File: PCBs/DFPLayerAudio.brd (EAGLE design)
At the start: 45.4 x 33 mm, 13 parts

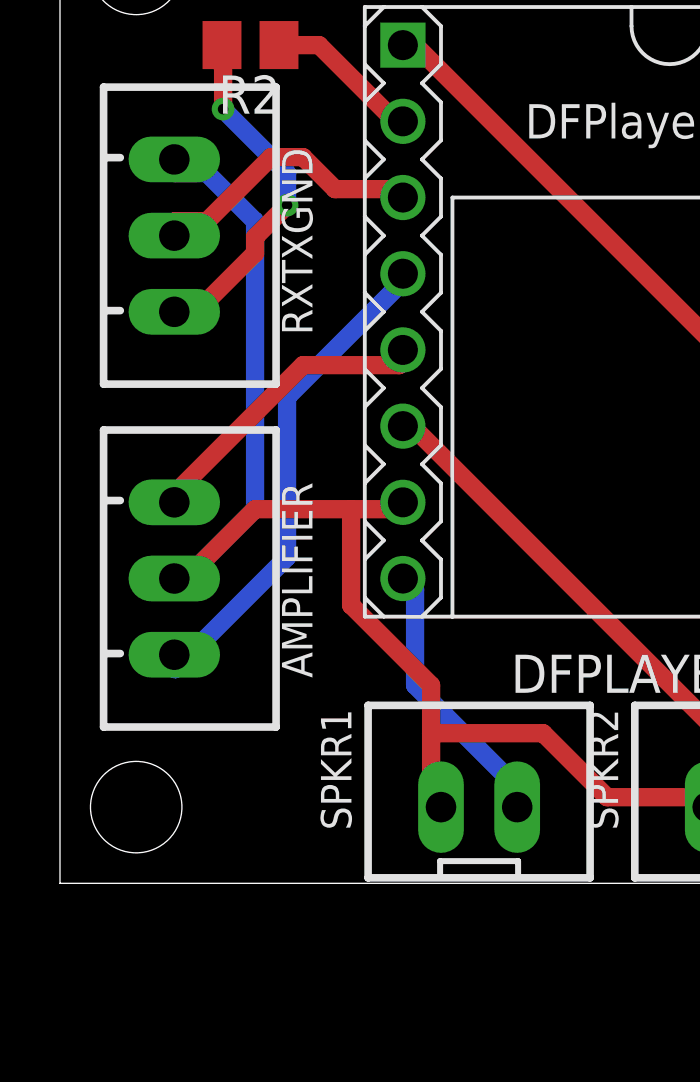
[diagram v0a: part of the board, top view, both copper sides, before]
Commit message: TX and Rx pin updated with resistor
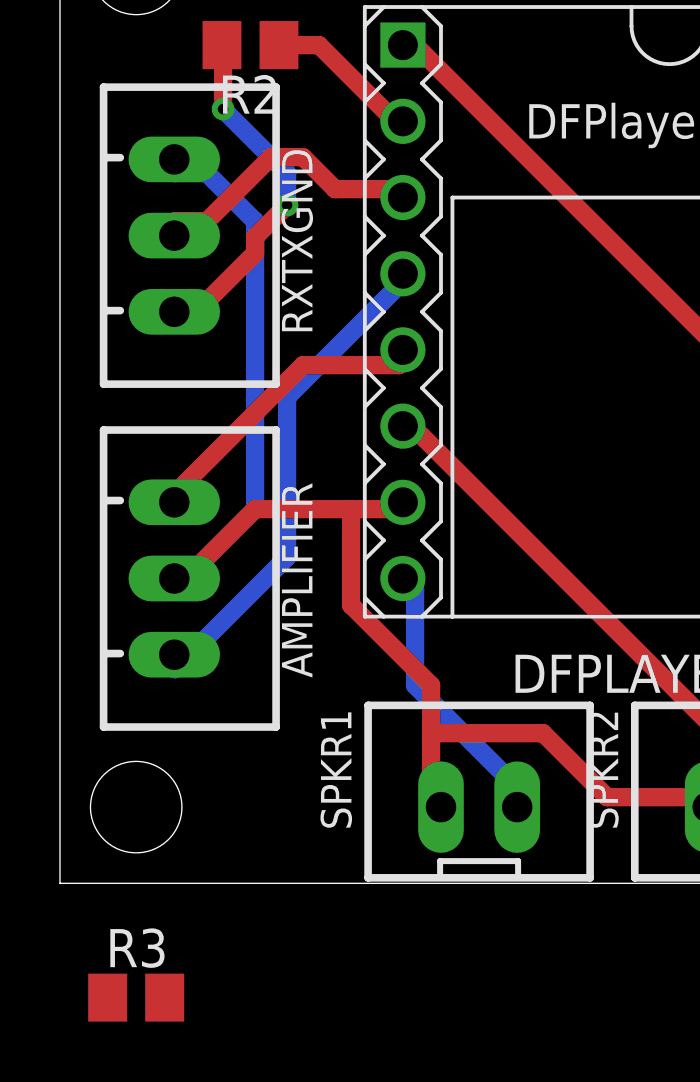
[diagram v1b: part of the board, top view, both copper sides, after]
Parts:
- added R3: 1K, adafruit:M0805
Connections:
- new net N$4: DFPLAYER.3, R3.1
- net N$2: now also R3.2; no longer DFPLAYER.3
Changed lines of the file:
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@@
 <drawing>
 <settings>
-<setting alwaysvectorfont="yes"/>
+<setting alwaysvectorfont="no"/>
 <setting verticaltext="up"/>
 </settings>
@@
 <attribute name="VALUE" x="77.3875" y="9.3975" size="1.016" layer="27" ratio="10" rot="R90"/>
 </element>
+<element name="R3" library="adafruit" package="M0805" value="1K" x="41.91" y="-5.08" smashed="yes">
+<attribute name="NAME" x="40.894" y="-4.064" size="1.27" layer="25"/>
+<attribute name="VALUE" x="40.894" y="-7.366" size="1.27" layer="27"/>
+</element>
 </elements>
 <signals>
@@
 <signal name="N$2">
 <contactref element="RXTXGND" pad="2"/>
-<contactref element="DFPLAYER" pad="3"/>
 <wire x1="48.5394" y1="21.8694" x2="50.673" y2="21.8694" width="0.6096" layer="1"/>
 <wire x1="47.4726" y1="22.9362" x2="48.5394" y2="21.8694" width="0.6096" layer="1"/>
@@
 <wire x1="44.2722" y1="20.8026" x2="46.4058" y2="22.9362" width="0.6096" layer="1"/>
 <wire x1="43.2054" y1="20.8026" x2="44.2722" y2="20.8026" width="0.6096" layer="1"/>
-<wire x1="50.673" y1="21.8694" x2="50.8" y2="21.59" width="0.6096" layer="1"/>
 <wire x1="43.2054" y1="20.8026" x2="43.18" y2="20.32" width="0.6096" layer="1"/>
+<contactref element="R3" pad="2"/>
+<wire x1="42.86" y1="-5.08" x2="43.18" y2="20.32" width="0" layer="19" extent="1-1"/>
+</signal>
+<signal name="N$4">
+<contactref element="R3" pad="1"/>
+<contactref element="DFPLAYER" pad="3"/>
+<wire x1="40.96" y1="-5.08" x2="50.8" y2="21.59" width="0" layer="19" extent="1-1"/>
 </signal>
 </signals>

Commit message: updated board
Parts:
- moved R3 32.2 mm to (47.0, 26.7), turned to 180 degrees
- moved R2 3.59 mm to (48.3, 29.2)
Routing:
- net N$5: track 5.29 -> 12.8 mm, vias 0 -> 1
- net N$4: track 0.00 -> 7.01 mm
- net GND: track 132.2 -> 138.3 mm
- net N$8: track 12.0 -> 17.7 mm
- net VCC: track 64.0 -> 66.5 mm
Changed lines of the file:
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@@
 <attribute name="VALUE" x="74.66" y="15.87" size="1.016" layer="27" rot="R180"/>
 </element>
-<element name="R2" library="adafruit" package="M0805" value="1K" x="45.72" y="26.67" smashed="yes" rot="R180">
-<attribute name="NAME" x="46.736" y="25.654" size="1.27" layer="25" rot="R180"/>
-<attribute name="VALUE" x="46.736" y="28.956" size="1.27" layer="27" rot="R180"/>
+<element name="R2" library="adafruit" package="M0805" value="1K" x="48.26" y="29.21" smashed="yes" rot="R180">
+<attribute name="NAME" x="49.276" y="28.194" size="1.27" layer="25" rot="R180"/>
+<attribute name="VALUE" x="49.276" y="31.496" size="1.27" layer="27" rot="R180"/>
 </element>
 <element name="5V" library="Rembrandt Electronics - JST XH Connectors v1-0" package="JST-XH-02-PACKAGE-LONG-PAD" value="JST-XH-02-PIN-LONG-PAD" x="81.28" y="12.7" smashed="yes" rot="R90">
@@
 <attribute name="VALUE" x="77.3875" y="9.3975" size="1.016" layer="27" ratio="10" rot="R90"/>
 </element>
-<element name="R3" library="adafruit" package="M0805" value="1K" x="41.91" y="-5.08" smashed="yes">
-<attribute name="NAME" x="40.894" y="-4.064" size="1.27" layer="25"/>
-<attribute name="VALUE" x="40.894" y="-7.366" size="1.27" layer="27"/>
+<element name="R3" library="adafruit" package="M0805" value="1K" x="46.99" y="26.67" smashed="yes" rot="R180">
+<attribute name="NAME" x="48.006" y="25.654" size="1.27" layer="25" rot="R180"/>
+<attribute name="VALUE" x="48.006" y="28.956" size="1.27" layer="27" rot="R180"/>
 </element>
 </elements>
@@
 <wire x1="75.7428" y1="8.001" x2="76.2" y2="7.54" width="0.6096" layer="1"/>
 <wire x1="74.1426" y1="5.8674" x2="68.58" y2="11.43" width="0.6096" layer="16"/>
-<wire x1="70.9422" y1="26.67" x2="72.66" y2="26.67" width="0.6096" layer="1"/>
-<wire x1="69.342" y1="28.2702" x2="70.9422" y2="26.67" width="0.6096" layer="1"/>
-<wire x1="67.7418" y1="28.2702" x2="69.342" y2="28.2702" width="0.6096" layer="1"/>
-<wire x1="66.675" y1="27.2034" x2="67.7418" y2="28.2702" width="0.6096" layer="1"/>
-<wire x1="66.675" y1="13.335" x2="66.675" y2="27.2034" width="0.6096" layer="1"/>
-<wire x1="68.58" y1="11.43" x2="66.675" y2="13.335" width="0.6096" layer="1"/>
+<wire x1="72.2122" y1="26.67" x2="72.66" y2="26.67" width="0.6096" layer="1"/>
+<wire x1="69.342" y1="29.5402" x2="72.2122" y2="26.67" width="0.6096" layer="1"/>
+<wire x1="66.4718" y1="29.5402" x2="69.342" y2="29.5402" width="0.6096" layer="1"/>
+<wire x1="64.135" y1="27.2034" x2="66.4718" y2="29.5402" width="0.6096" layer="1"/>
+<wire x1="64.135" y1="13.335" x2="64.135" y2="27.2034" width="0.6096" layer="1"/>
+<wire x1="68.58" y1="11.43" x2="66.04" y2="11.43" width="0.6096" layer="1"/>
+<wire x1="66.04" y1="11.43" x2="64.135" y2="13.335" width="0.6096" layer="1"/>
 <wire x1="45.8724" y1="11.2014" x2="49.0728" y2="11.2014" width="0.6096" layer="1"/>
 <wire x1="49.0728" y1="11.2014" x2="50.673" y2="11.2014" width="0.6096" layer="1"/>
@@
 <wire x1="69.8754" y1="3.7338" x2="69.53" y2="3.81" width="0.6096" layer="1"/>
 <wire x1="74.676" y1="13.8684" x2="74.66" y2="13.97" width="0.6096" layer="1"/>
-<wire x1="66.675" y1="11.2014" x2="51.2064" y2="26.67" width="0.6096" layer="1"/>
-<wire x1="66.675" y1="7.4676" x2="66.675" y2="11.2014" width="0.6096" layer="1"/>
-<wire x1="69.8754" y1="4.2672" x2="66.675" y2="7.4676" width="0.6096" layer="1"/>
-<wire x1="51.2064" y1="26.67" x2="50.8" y2="26.67" width="0.6096" layer="1"/>
+<wire x1="50.8" y1="26.67" x2="51.2064" y2="26.67" width="0.6096" layer="1"/>
 <wire x1="69.8754" y1="4.2672" x2="69.53" y2="3.81" width="0.6096" layer="1"/>
 <contactref element="5V" pad="1"/>
@@
 <wire x1="78.4098" y1="10.1346" x2="79.4766" y2="11.2014" width="0.6096" layer="1"/>
 <wire x1="81.0768" y1="11.2014" x2="81.28" y2="11.43" width="0.6096" layer="1"/>
+<wire x1="54.61" y1="23.2664" x2="54.61" y2="15.24" width="0.6096" layer="1"/>
+<wire x1="54.61" y1="15.24" x2="62.23" y2="7.62" width="0.6096" layer="1"/>
+<wire x1="51.2064" y1="26.67" x2="54.61" y2="23.2664" width="0.6096" layer="1"/>
+<wire x1="62.23" y1="7.62" x2="66.5226" y2="7.62" width="0.6096" layer="1"/>
+<wire x1="66.5226" y1="7.62" x2="69.8754" y2="4.2672" width="0.6096" layer="1"/>
 </signal>
 <signal name="N$5">
 <contactref element="DFPLAYER" pad="2"/>
 <contactref element="R2" pad="1"/>
-<wire x1="48.006" y1="26.67" x2="46.67" y2="26.67" width="0.6096" layer="1"/>
-<wire x1="50.673" y1="24.003" x2="48.006" y2="26.67" width="0.6096" layer="1"/>
-<wire x1="50.673" y1="24.003" x2="50.8" y2="24.13" width="0.6096" layer="1"/>
+<wire x1="53.34" y1="29.21" x2="54.61" y2="27.94" width="0.6096" layer="1"/>
+<wire x1="54.61" y1="27.94" x2="54.61" y2="25.4" width="0.6096" layer="1"/>
+<wire x1="49.21" y1="29.21" x2="53.34" y2="29.21" width="0.6096" layer="1"/>
+<via x="54.61" y="25.4" extent="1-16" drill="0.35"/>
+<wire x1="54.61" y1="25.4" x2="53.34" y2="24.13" width="0.6096" layer="16"/>
+<wire x1="53.34" y1="24.13" x2="50.8" y2="24.13" width="0.6096" layer="16"/>
 </signal>
 <signal name="N$14">
@@
 <contactref element="R2" pad="2"/>
 <contactref element="RXTXGND" pad="3"/>
-<wire x1="44.8056" y1="24.5364" x2="44.8056" y2="26.67" width="0.6096" layer="1"/>
+<wire x1="44.196" y1="25.146" x2="44.8056" y2="24.5364" width="0.6096" layer="1"/>
 <wire x1="46.9392" y1="22.4028" x2="44.8056" y2="24.5364" width="0.6096" layer="16"/>
 <wire x1="46.9392" y1="21.336" x2="46.9392" y2="22.4028" width="0.6096" layer="16"/>
-<wire x1="45.8724" y1="20.2692" x2="46.9392" y2="21.336" width="0.6096" layer="1"/>
-<wire x1="45.8724" y1="19.7358" x2="45.8724" y2="20.2692" width="0.6096" layer="1"/>
-<wire x1="44.2722" y1="18.1356" x2="45.8724" y2="19.7358" width="0.6096" layer="1"/>
-<wire x1="43.2054" y1="18.1356" x2="44.2722" y2="18.1356" width="0.6096" layer="1"/>
-<wire x1="44.8056" y1="26.67" x2="44.77" y2="26.67" width="0.6096" layer="1"/>
-<wire x1="43.2054" y1="18.1356" x2="43.18" y2="17.78" width="0.6096" layer="1"/>
 <via x="44.8056" y="24.5364" extent="1-16" drill="0.35"/>
 <via x="46.9392" y="21.336" extent="1-16" drill="0.35"/>
+<wire x1="44.196" y1="25.146" x2="44.196" y2="27.47284375" width="0.6096" layer="1"/>
+<wire x1="45.93315625" y1="29.21" x2="47.31" y2="29.21" width="0.6096" layer="1"/>
+<wire x1="44.196" y1="27.47284375" x2="45.93315625" y2="29.21" width="0.6096" layer="1"/>
+<wire x1="46.9392" y1="21.336" x2="46.99" y2="21.2852" width="0.6096" layer="1"/>
+<wire x1="46.99" y1="21.2852" x2="46.99" y2="19.05" width="0.6096" layer="1"/>
+<wire x1="46.99" y1="19.05" x2="45.72" y2="17.78" width="0.6096" layer="1"/>
+<wire x1="45.72" y1="17.78" x2="43.18" y2="17.78" width="0.6096" layer="1"/>
 </signal>
 <signal name="N$1">
@@
 <signal name="N$2">
 <contactref element="RXTXGND" pad="2"/>
-<wire x1="48.5394" y1="21.8694" x2="50.673" y2="21.8694" width="0.6096" layer="1"/>
-<wire x1="47.4726" y1="22.9362" x2="48.5394" y2="21.8694" width="0.6096" layer="1"/>
-<wire x1="46.4058" y1="22.9362" x2="47.4726" y2="22.9362" width="0.6096" layer="1"/>
-<wire x1="44.2722" y1="20.8026" x2="46.4058" y2="22.9362" width="0.6096" layer="1"/>
-<wire x1="43.2054" y1="20.8026" x2="44.2722" y2="20.8026" width="0.6096" layer="1"/>
-<wire x1="43.2054" y1="20.8026" x2="43.18" y2="20.32" width="0.6096" layer="1"/>
 <contactref element="R3" pad="2"/>
-<wire x1="42.86" y1="-5.08" x2="43.18" y2="20.32" width="0" layer="19" extent="1-1"/>
+<wire x1="43.18" y1="20.32" x2="44.45" y2="20.32" width="0.6096" layer="1"/>
+<wire x1="45.799" y1="21.669" x2="45.799" y2="21.8082875" width="0.6096" layer="1"/>
+<wire x1="46.99" y1="22.9992875" x2="46.99" y2="24.13" width="0.6096" layer="1"/>
+<wire x1="45.799" y1="21.8082875" x2="46.99" y2="22.9992875" width="0.6096" layer="1"/>
+<wire x1="46.99" y1="24.13" x2="45.72" y2="25.4" width="0.6096" layer="1"/>
+<wire x1="45.72" y1="25.4" x2="45.72" y2="26.35" width="0.6096" layer="1"/>
+<wire x1="45.72" y1="26.35" x2="46.04" y2="26.67" width="0.6096" layer="1"/>
+<wire x1="44.45" y1="20.32" x2="45.799" y2="21.669" width="0.6096" layer="1"/>
 </signal>
 <signal name="N$4">
 <contactref element="R3" pad="1"/>
 <contactref element="DFPLAYER" pad="3"/>
-<wire x1="40.96" y1="-5.08" x2="50.8" y2="21.59" width="0" layer="19" extent="1-1"/>
+<wire x1="47.94" y1="26.67" x2="48.26" y2="26.35" width="0.6096" layer="1"/>
+<wire x1="48.26" y1="26.35" x2="48.26" y2="22.86" width="0.6096" layer="1"/>
+<wire x1="48.26" y1="22.86" x2="49.53" y2="21.59" width="0.6096" layer="1"/>
+<wire x1="49.53" y1="21.59" x2="50.8" y2="21.59" width="0.6096" layer="1"/>
 </signal>
 </signals>
